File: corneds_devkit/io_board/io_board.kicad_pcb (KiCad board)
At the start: 2 copper layers, 144 x 114 mm, 36 parts, among them J1 Conn_01x09_Pin, J2 JOY_VSEL, SW1 SW_Push, SW10 SW_Push, SW11 SW_Push, SW12 SW_Push, SW13 SW_Push, SW15 SW_Push, SW17 SW_Push, SW19 SW_Push, SW2 SW_Push, SW20 SW_Push, SW21 SW_Push, SW22 SW_Push, SW23 SW_Push, SW24 SW_Push, SW3 SW_Push, SW4 SW_Push, SW43 SW_Push, SW5 SW_Push, SW6 SW_Push, SW7 SW_Push, SW8 SW_Push, SW9 SW_Push, U1 COM-09426

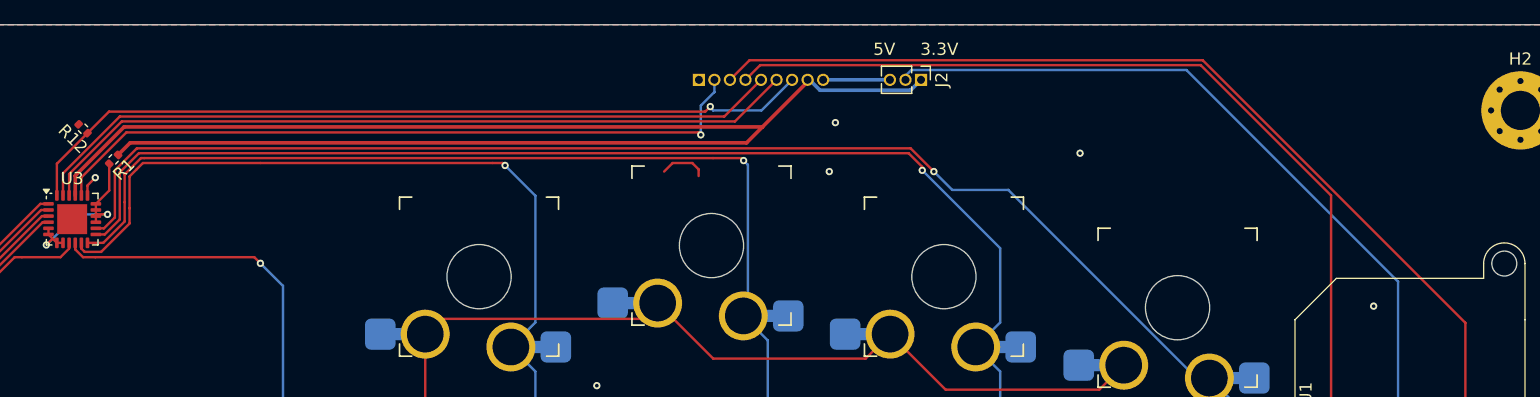
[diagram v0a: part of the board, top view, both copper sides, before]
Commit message: replaced io board headers with 2.54mm and added pullups to i2c lines
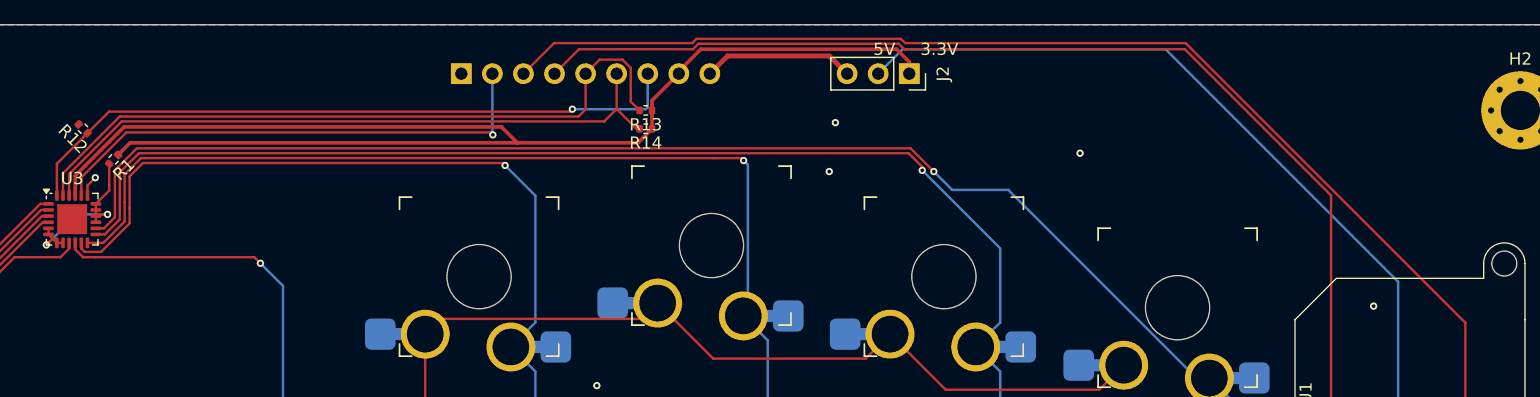
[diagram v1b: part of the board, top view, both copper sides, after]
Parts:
- added R13: 4.7k, Resistor_SMD:R_0402_1005Metric, F.Cu at (53.5, 46.5)
- added R14: 4.7k, Resistor_SMD:R_0402_1005Metric, F.Cu at (53.5, 48.0)
- J1: footprint Connector_PinHeader_1.27mm:PinHeader_1x09_P1.27mm_Vertical -> Connector_PinSocket_2.54mm:PinSocket_1x09_P2.54mm_Vertical
- J2: footprint Connector_PinHeader_1.27mm:PinHeader_1x03_P1.27mm_Vertical -> Connector_PinSocket_2.54mm:PinSocket_1x03_P2.54mm_Vertical
- moved J1 19.4 mm to (38.4, 43.5)
- moved J2 1.08 mm to (75.0, 43.5)
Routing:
- net Net-(J1-Pin_3): track 95.2 -> 113.3 mm
- net VDD_3V3: track 128.3 -> 111.1 mm
- net nRESET: track 58.7 -> 41.7 mm
- net Net-(J1-Pin_4): track 89.8 -> 106.6 mm
- net nINT: track 65.8 -> 55.5 mm
- net SDA: track 62.8 -> 54.1 mm
- net VDD_5V: track 5.46 -> 12.4 mm
- net SCL: track 62.0 -> 57.8 mm
- net GND: track 5.59 -> 1.72 mm
- net VJOY: track 65.1 -> 68.3 mm
